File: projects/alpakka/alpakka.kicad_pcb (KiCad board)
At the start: 2 copper layers, 130 x 51 mm, 82 parts, among them P1 Conn_01x20_Pin, P2 Conn_01x20_Pin, P3 Conn_01x04, P4 Blade, P6 Conn_01x02, U1 Alpsalpine_RKJXV, U10 ST_LSM6, U12 ST_LSM6, U2 Alpsalpine_RKJXV, U3 Alpsalpine_EC10E, U6 NXP_PCAL6416A, U8 NXP_PCAL6416A

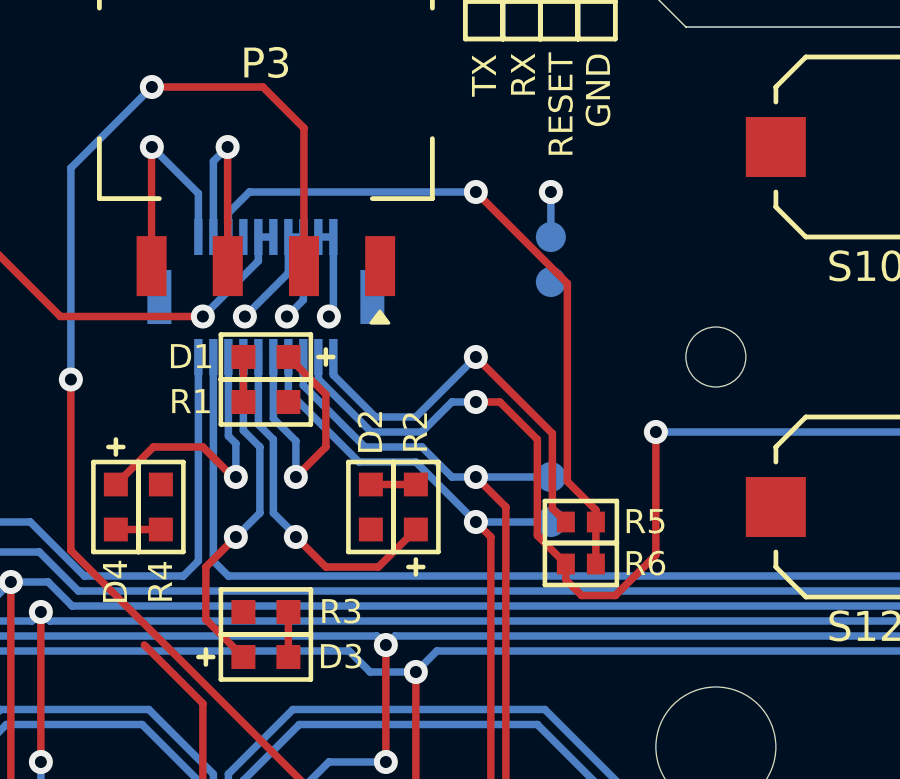
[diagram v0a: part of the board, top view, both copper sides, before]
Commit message: Alpakka revert to single touch path, Shifted GPIOs to match Marmota
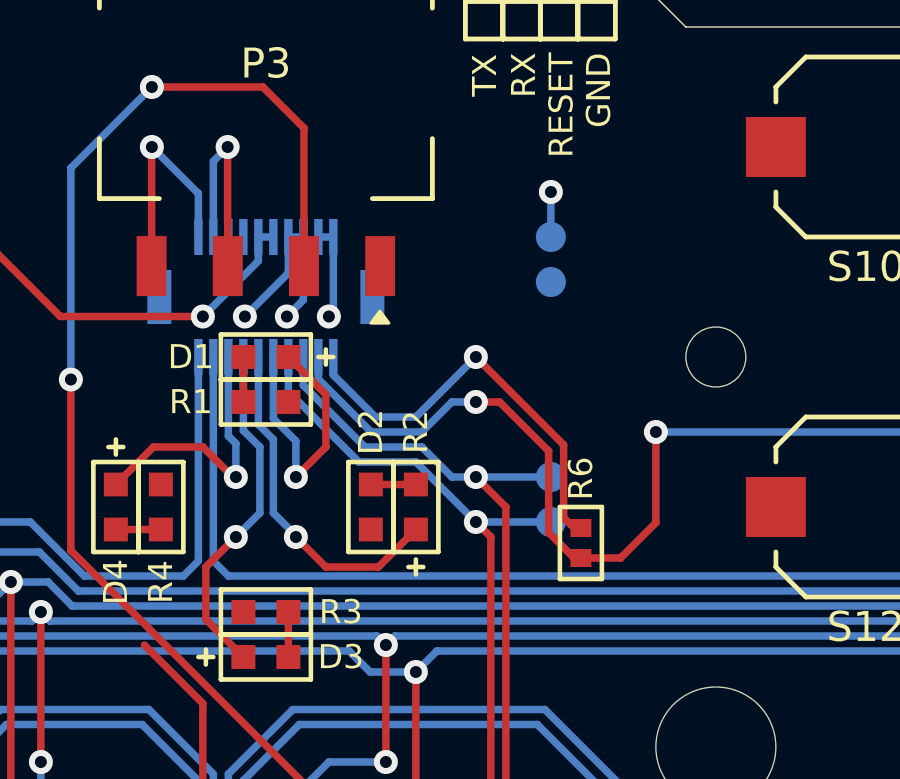
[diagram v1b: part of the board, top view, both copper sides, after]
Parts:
- removed R5: 1 MΩ, ILO_fp:0402
- moved R6 0.70 mm to (110.5, 55.2), turned to 90 degrees
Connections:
- D1 pad 2: /GP10 -> /GP9
- D2 pad 2: /GP9 -> /GP8
- D3 pad 2: /GP8 -> /GP7
- D4 pad 2: /GP7 -> /GP6
- P1 pad 13: /GP7 -> /GP6
- P1 pad 14: /GP8 -> /GP7
- P1 pad 15: /GP9 -> /GP8
- P1 pad 16: /GP10 -> /GP9
- P1 pad 17: /GP11 -> /GP10
- P1 pad 18: /GP12 -> /GP11
- P1 pad 19: /GP13 -> /GP12
- P1 pad 20: /GP14 -> /GP13
- P1 pad 3: /GP4 -> unconnected-(P1-Pin_3-Pad3)
- P4 pad 1: /GP13 -> /GP12
- R6 pad 1: /GP13 -> /GP12
- R6 pad 2: /GP4 -> /GP13
- TPS0 pad 1: /GP11 -> /GP10
- TPS1 pad 1: /GP12 -> /GP11
- U3 pad 1: /GP11 -> /GP10
- U3 pad 2: /GP12 -> /GP11
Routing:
- net /GP13: track 62.7 -> 14.0 mm, vias 3 -> 1
- net /GP10: track 9.24 -> 36.8 mm
- net /GP12: track 35.5 -> 60.5 mm, vias 1 -> 3
- net /GP4: track 23.5 -> 0.00 mm, vias 1 -> 0
- net /GP14: track 13.5 -> 0.00 mm, vias 1 -> 0
- net /GP6: track 0.00 -> 9.04 mm, vias 0 -> 1
- net /GP7: track 9.04 -> 11.5 mm
- net /GP9: track 11.4 -> 9.24 mm
- net /GP11: track 36.8 -> 35.5 mm

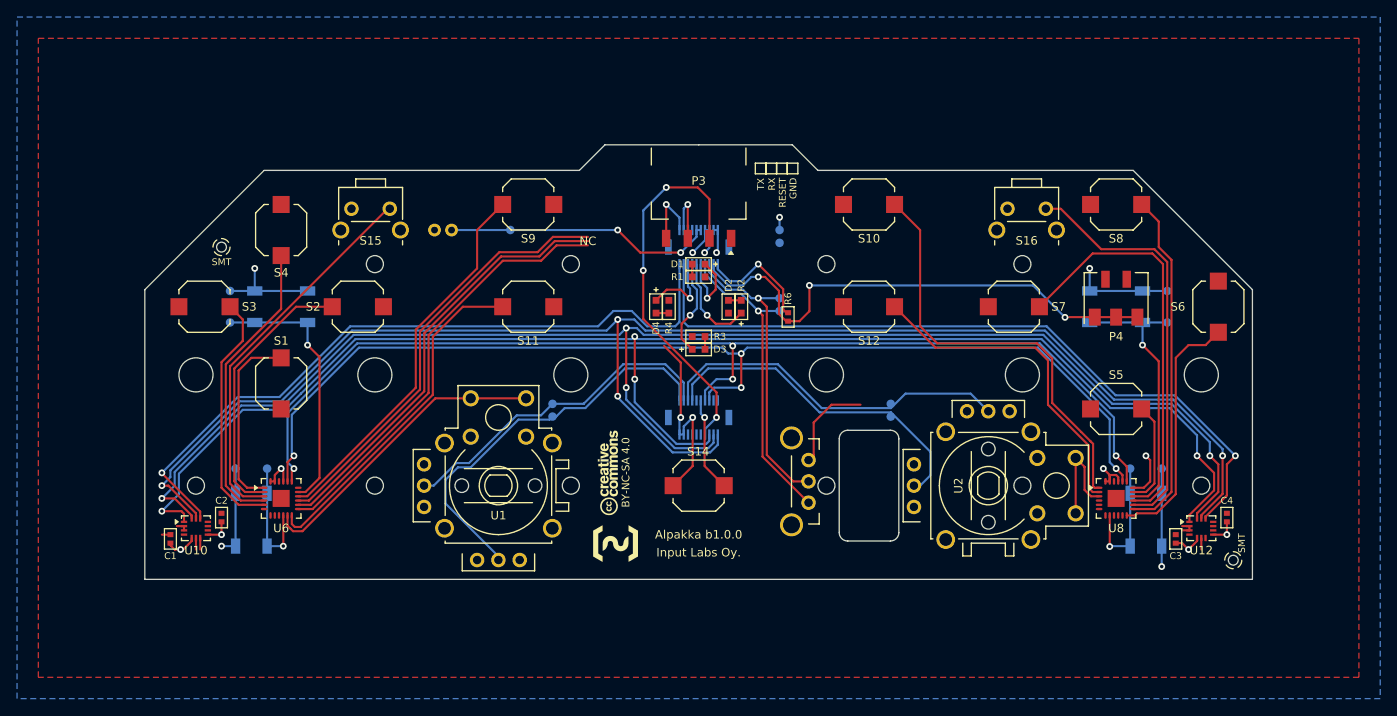
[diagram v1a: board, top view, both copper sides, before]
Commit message: Alpakka edge rails, USB indication silkscreen
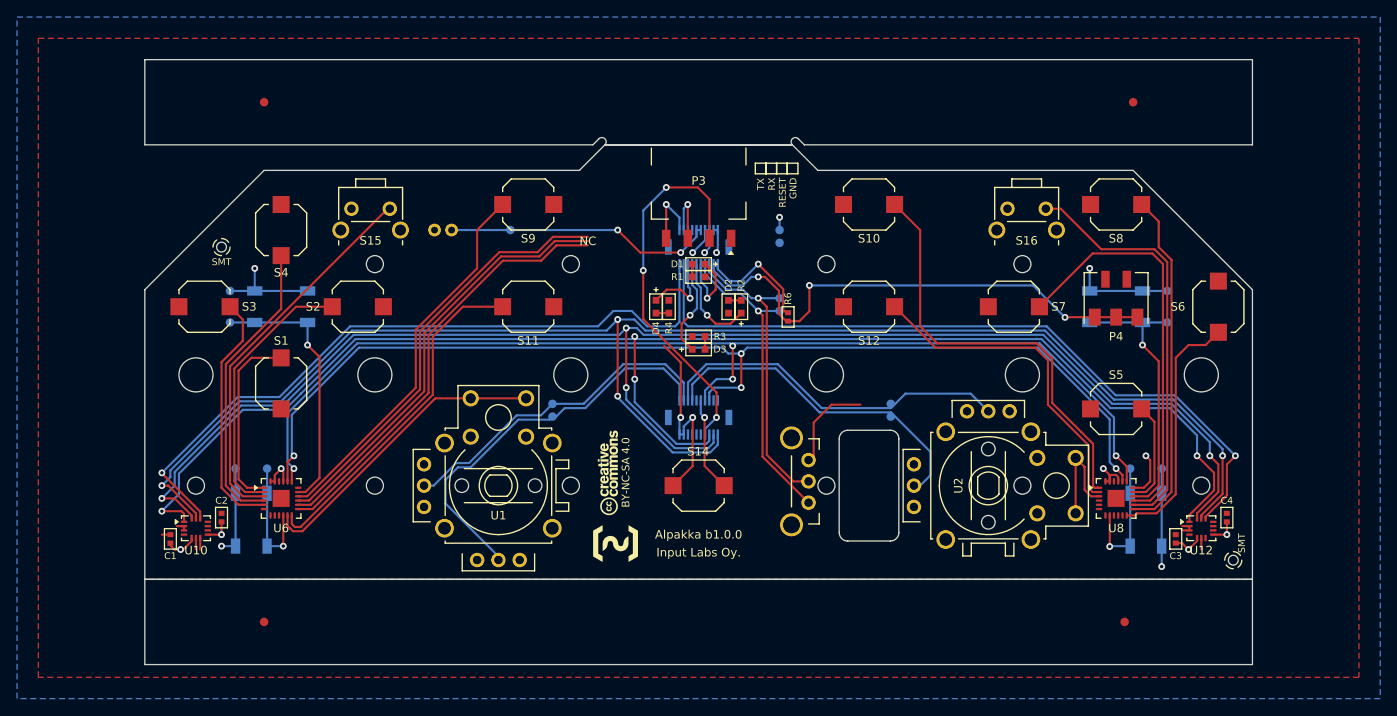
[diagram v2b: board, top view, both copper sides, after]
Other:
- board size 130 x 51 mm -> 130 x 71 mm
- board text added: "--V-CUT"
- board text added: "USB (DNP)"
- board text added: "V-CUT--"

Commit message: Reworked Alpakka w/ interrupt lines, etc
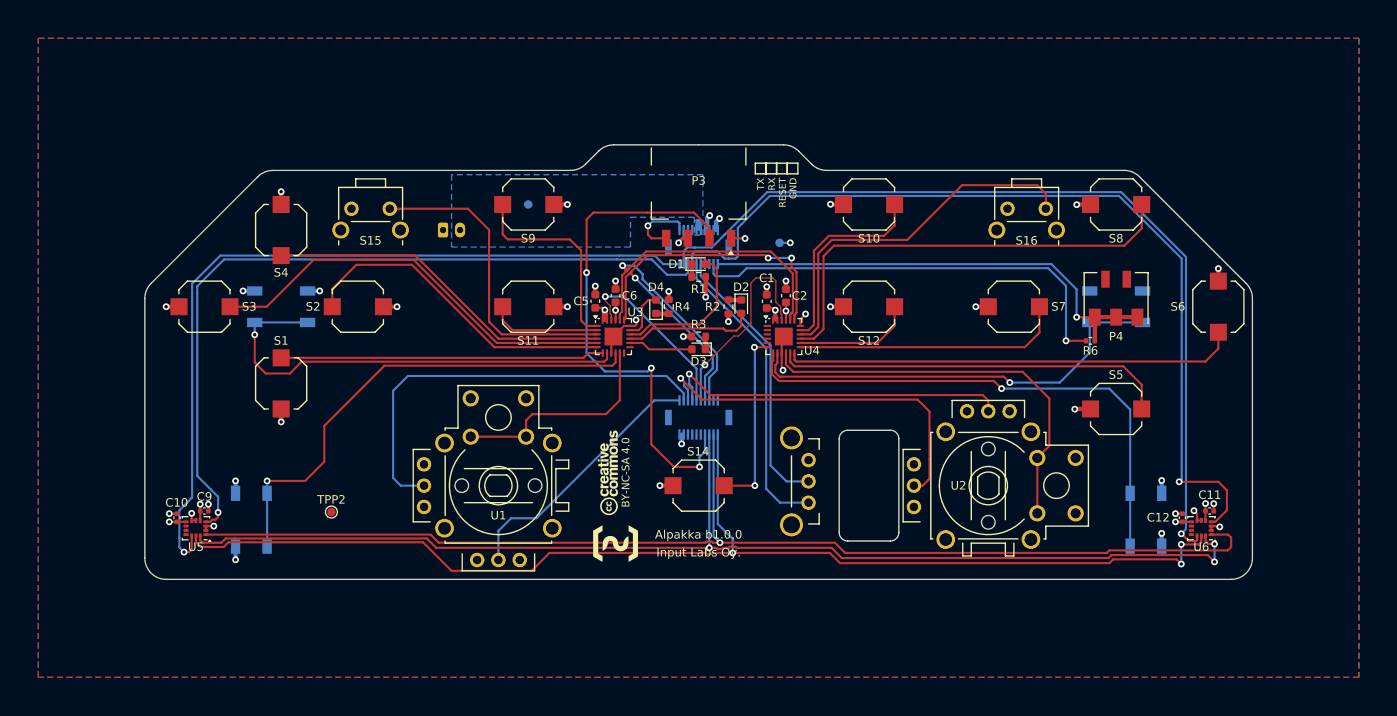
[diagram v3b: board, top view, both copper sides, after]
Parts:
- removed ?: , 
- removed C3, C4: 100nF, ILO_fp:0402
- removed REF** (x6): NPTH_4mm, ILO_fp:NPTH_4mm
- removed REF** (x11): NPTH_2mm, ILO_fp:NPTH_2mm
- removed TP101, TP102, TP103, TP104, TP201, TP202, TP203, TP204, TPA0, TPA1, TPA2, TPA3, TPBAT0, TPP0, TPS0, TPS1: Endpoint, ILO_fp:Pad_1mm
- added C10: 100nF, Capacitor_SMD:C_0402_1005Metric, F.Cu at (38.8, 78.8)
- added C11: 100nF, Capacitor_SMD:C_0402_1005Metric, F.Cu at (160.0, 78.0)
- added C12: 100nF, Capacitor_SMD:C_0402_1005Metric, F.Cu at (156.8, 78.8)
- added C5: 4.7uF, Capacitor_SMD:C_0603_1608Metric, F.Cu at (87.9, 53.4)
- added C6: 4.7uF, Capacitor_SMD:C_0603_1608Metric, F.Cu at (90.2, 52.7)
- added C9: 100nF, Capacitor_SMD:C_0402_1005Metric, F.Cu at (42.0, 78.0)
- added TPP2: Endpoint, TestPoint:TestPoint_Pad_D1.0mm, F.Cu at (56.9, 78.1)
- added TPP3: Endpoint, TestPoint:TestPoint_Pad_D1.0mm, B.Cu at (80.0, 42.0)
- C1, C2: value 100nF -> 4.7uF; footprint ILO_fp:0402 -> Capacitor_SMD:C_0603_1608Metric
- D1, D2, D3, D4: footprint ILO_fp:0603_d -> Diode_SMD:D_0603_1608Metric
- P6: footprint ILO_fp:JST_PH_2_TH -> Connector_JST:JST_PH_S2B-PH-K_1x02_P2.00mm_Horizontal
- R1, R2, R3, R4: footprint ILO_fp:0603 -> Resistor_SMD:R_0603_1608Metric
- R6: footprint ILO_fp:0402 -> Resistor_SMD:R_0402_1005Metric
- SW1: renamed from U3; value Alpsalpine_EC10E -> EC10E
- TPP1: footprint ILO_fp:Pad_1mm -> TestPoint:TestPoint_Pad_D1.0mm
- U3: renamed from U6; value NXP_PCAL6416A -> PCAL6416AHF; footprint ILO_fp:QFN24 -> Package_DFN_QFN:HVQFN-24-1EP_4x4mm_P0.5mm_EP2.1x2.1mm
- U4: renamed from U8; value NXP_PCAL6416A -> PCAL6416AHF; footprint ILO_fp:QFN24 -> Package_DFN_QFN:HVQFN-24-1EP_4x4mm_P0.5mm_EP2.1x2.1mm
- U5: renamed from U10; value ST_LSM6 -> LSM6DSL; footprint ILO_fp:LGA14 -> Package_LGA:LGA-14_3x2.5mm_P0.5mm_LayoutBorder3x4y
- U6: renamed from U12; value ST_LSM6 -> LSM6DSL; footprint ILO_fp:LGA14 -> Package_LGA:LGA-14_3x2.5mm_P0.5mm_LayoutBorder3x4y
- moved C1 75.3 mm to (108.0, 53.4), turned to 90 degrees
- moved C2 71.2 mm to (110.2, 52.7), turned to 90 degrees
- moved U3 43.4 mm to (90.0, 57.5), turned to 0 degrees
- moved U4 43.4 mm to (110.0, 57.5), turned to 0 degrees
- moved R6 35.6 mm to (146.0, 58.0), turned to 180 degrees
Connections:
- net /A2 renamed /B_L1
- net /A3 renamed /B_UP
- net /A4 renamed /B_LEFT
- net /A8 renamed /B_L4
- net /ADC2 renamed /LSTICK_X
- net /ADC3 renamed /LSTICK_Y
- net /B10 renamed /B_B
- net /BAT renamed VBAT
- net /IMU_CS0 renamed /IMU0_~{CS}
- net /IMU_CS1 renamed /IMU1_~{CS}
- net /SPI_CK renamed /SPI_SCK
- C1 pad 1: /GND -> VDD
- C1 pad 2: /VCC -> GND
- C2 pad 1: /GND -> VDD
- C2 pad 2: /VCC -> GND
- D1 pad 2: /GP9 -> /LED1
- D2 pad 2: /GP8 -> /LED2
- D3 pad 2: /GP7 -> /LED3
- D4 pad 2: /GP6 -> /LED4
- P1 pad 10: /VCC -> VDD
- P1 pad 13: /GP6 -> /IMU0_~{INT}
- P1 pad 14: /GP7 -> /IMU1_~{INT}
- P1 pad 15: /GP8 -> /SCROLL_A
- P1 pad 16: /GP9 -> /SCROLL_B
- P1 pad 19: /GP12 -> /TOUCH_STIM
- P1 pad 20: /GP13 -> /TOUCH_MEAS
- P1 pad 7: /GND -> GND
- P1 pad 8: /GND -> GND
- P1 pad 9: /VCC -> VDD
- P2 pad 11: /GND -> GND
- P2 pad 12: /GND -> GND
- P2 pad 18: /SPI_RX -> /SPI_SDO
- P2 pad 19: /SPI_TX -> /SPI_SDI
- P2 pad 3: /ADC1 -> /RSTICK_Y
- P2 pad 4: /ADC0 -> /RSTICK_X
- P2 pad 5: /GP25 -> /EXP0_~{INT}
- P2 pad 6: /GP24 -> /EXP1_~{INT}
- P3 pad 1: /GND -> GND
- P4 pad 1: /GP12 -> /TOUCH_MEAS
- P6 pad 1: /GND -> GND
- R1 pad 1: /GND -> GND
- R2 pad 1: /GND -> GND
- R3 pad 1: /GND -> GND
- R4 pad 1: /GND -> GND
- R6 pad 1: /GP12 -> /TOUCH_MEAS
- R6 pad 2: /GP13 -> /TOUCH_STIM
- S1 pad 1: /GND -> GND
- S1 pad 2: /A0 -> /B_DOWN
- S10 pad 1: /GND -> GND
- S10 pad 2: /B0 -> /B_START1
- S11 pad 1: /GND -> GND
- S11 pad 2: /A10 -> /B_SEL2
- S12 pad 1: /GND -> GND
- S12 pad 2: /B1 -> /B_START2
- S14 pad 1: /GND -> GND
- S14 pad 2: /GP24 -> /B_HOME
- S15 pad 1: /GND -> GND
- S16 pad 1: /GND -> GND
- S16 pad 2: /B12 -> /B_R1
- S17 pad 1: /GND -> GND
- S17 pad 2: /A15 -> /B_L2
- S18 pad 1: /GND -> GND
- S18 pad 2: /B14 -> /B_R2
- S19 pad 1: /GND -> GND
- S2 pad 1: /GND -> GND
- S2 pad 2: /A1 -> /B_RIGHT
- S20 pad 1: /GND -> GND
- S20 pad 2: /B7 -> /B_R4
- S3 pad 1: /GND -> GND
- S4 pad 1: /GND -> GND
- S5 pad 1: /GND -> GND
- S5 pad 2: /B15 -> /B_A
- S6 pad 1: /GND -> GND
- S7 pad 1: /GND -> GND
- S7 pad 2: /B13 -> /B_X
- S8 pad 1: /GND -> GND
- S8 pad 2: /B11 -> /B_Y
- S9 pad 1: /GND -> GND
- S9 pad 2: /A14 -> /B_SEL1
- TPP1 pad 1: /VCC -> VDD
- U1 pad 1: /GND -> GND
- U1 pad 10: /A9 -> GND
- U1 pad 3: /VCC -> VDD
- U1 pad 4: /GND -> GND
- U1 pad 6: /VCC -> VDD
- U1 pad 7: /GND -> /LSTICK_PUSH
- U1 pad 8: /A9 -> GND
- U1 pad 9: /GND -> /LSTICK_PUSH
- U2 pad 1: /GND -> GND
- U2 pad 10: /B2 -> GND
- U2 pad 2: /ADC1 -> /RSTICK_X
- U2 pad 3: /VCC -> VDD
- U2 pad 4: /GND -> GND
- U2 pad 5: /ADC0 -> /RSTICK_Y
- U2 pad 6: /VCC -> VDD
- U2 pad 7: /GND -> /RSTICK_PUSH
- U2 pad 8: /B2 -> GND
- U2 pad 9: /GND -> /RSTICK_PUSH
- U3 pad 1: /A0 -> /B_SEL1
- U3 pad 11: /A9 -> /LSTICK_PUSH
- U3 pad 12: /A10 -> unconnected-(U3-P1_2-Pad12)
- U3 pad 13: /A11 -> unconnected-(U3-P1_3-Pad13)
- U3 pad 14: /A12 -> /LED3
- U3 pad 15: /A13 -> /LED2
- U3 pad 16: /A14 -> /LED1
- U3 pad 17: /A15 -> /LED4
- U3 pad 18: /GND -> GND
- U3 pad 2: /A1 -> /B_SEL2
- U3 pad 21: /VCC -> VDD
- U3 pad 22: unconnected-(U6-INT-Pad22) -> /EXP0_~{INT}
- U3 pad 23: /VCC -> VDD
- U3 pad 24: /VCC -> VDD
- U3 pad 6: unconnected-(U6-P5-Pad6) -> /B_RIGHT
- U3 pad 7: /A6 -> /B_DOWN
- U3 pad 8: /A7 -> /B_L2
- U3 pad 9: /GND -> GND
- U4 pad 1: /B0 -> unconnected-(U4-P0_0-Pad1)
- U4 pad 10: unconnected-(U8-P8-Pad10) -> /RSTICK_PUSH
- U4 pad 11: unconnected-(U8-P9-Pad11) -> /B_A
- U4 pad 13: /B11 -> /B_X
- U4 pad 14: /B12 -> /B_START2
- U4 pad 15: /B13 -> /B_Y
- U4 pad 16: /B14 -> /B_R1
- U4 pad 17: /B15 -> /B_START1
- U4 pad 18: /VCC -> VDD
- U4 pad 2: /B1 -> unconnected-(U4-P0_1-Pad2)
- U4 pad 21: /VCC -> VDD
- U4 pad 22: unconnected-(U8-INT-Pad22) -> /EXP1_~{INT}
- U4 pad 23: /VCC -> VDD
- U4 pad 24: /VCC -> VDD
- U4 pad 3: /B2 -> unconnected-(U4-P0_2-Pad3)
- U4 pad 4: /B3 -> unconnected-(U4-P0_3-Pad4)
- U4 pad 5: /B4 -> unconnected-(U4-P0_4-Pad5)
- U4 pad 6: /B5 -> /B_HOME
- U4 pad 7: /B6 -> /B_R4
- U4 pad 8: /B7 -> /B_R2
- U4 pad 9: /GND -> GND
- U5 pad 1: /SPI_RX -> /SPI_SDI
- U5 pad 14: /SPI_TX -> /SPI_SDO
- U5 pad 2: /GND -> GND
- U5 pad 3: /GND -> GND
- U5 pad 4: unconnected-(U10-INT1-Pad4) -> /IMU0_~{INT}
- U5 pad 5: /VCC -> VDD
- U5 pad 6: /GND -> GND
- U5 pad 7: /GND -> GND
- U5 pad 8: /VCC -> VDD
- U6 pad 1: /SPI_RX -> /SPI_SDI
- U6 pad 14: /SPI_TX -> /SPI_SDO
- U6 pad 2: /GND -> GND
- U6 pad 3: /GND -> GND
- U6 pad 4: unconnected-(U12-INT1-Pad4) -> /IMU1_~{INT}
- U6 pad 5: /VCC -> VDD
- U6 pad 6: /GND -> GND
- U6 pad 7: /GND -> GND
- U6 pad 8: /VCC -> VDD
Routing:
- net /SPI_TX: track 175.1 -> 0.00 mm, vias 4 -> 0
- net /SPI_RX: track 171.4 -> 0.00 mm, vias 4 -> 0
- net /SPI_SDO: track 0.00 -> 138.7 mm, vias 0 -> 3
- net /SPI_SDI: track 0.00 -> 138.2 mm, vias 0 -> 1
- net /IMU1_~{INT}: track 0.00 -> 104.2 mm, vias 0 -> 1
- net /GND: track 96.5 -> 0.00 mm, vias 9 -> 0
- net /IMU0_~{INT}: track 0.00 -> 90.5 mm, vias 0 -> 1
- net /I2C_SCL: track 129.6 -> 53.4 mm, vias 4 -> 3
- net /I2C_SDA: track 128.4 -> 56.4 mm, vias 4 -> 1
- net GND: track 0.00 -> 62.9 mm, vias 0 -> 40
- net /B_R4: track 0.00 -> 62.3 mm, vias 0 -> 1
- net /GP12: track 60.5 -> 0.00 mm, vias 3 -> 0
- net /TOUCH_MEAS: track 0.00 -> 56.5 mm, vias 0 -> 1
- net /B_L2: track 0.00 -> 54.2 mm, vias 0 -> 1
- net /B_Y: track 0.00 -> 53.2 mm
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- added copper zone on B.Cu, net GND
- added copper zone on F.Cu, net GND
- added copper zone on In1.Cu, net GND
- added copper zone on B.Cu, net VBAT
- added copper zone on In2.Cu, net VDD
- removed copper zone on F.Cu, net /GND
- removed copper zone on B.Cu, net /VCC
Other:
- board size 130 x 71 mm -> 130 x 51 mm
- copper layers 2 -> 4
- board text removed: "--V-CUT"
- board text removed: "BAT"
- board text removed: "NC"
- board text removed: "SMT"
- board text removed: "TP"
- board text removed: "USB (DNP)"
- board text removed: "V-CUT--"

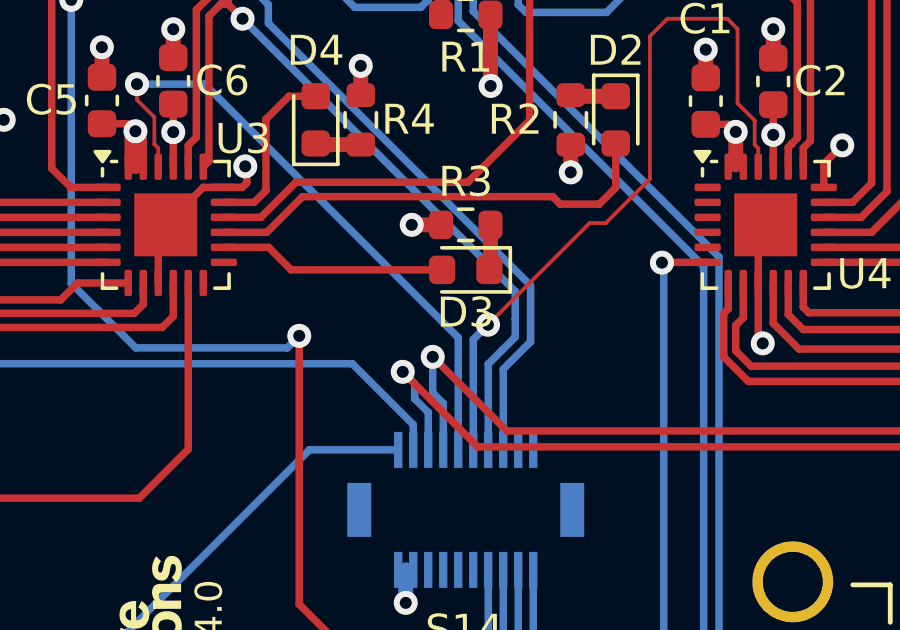
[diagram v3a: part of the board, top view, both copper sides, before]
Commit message: Updated for nRF52840
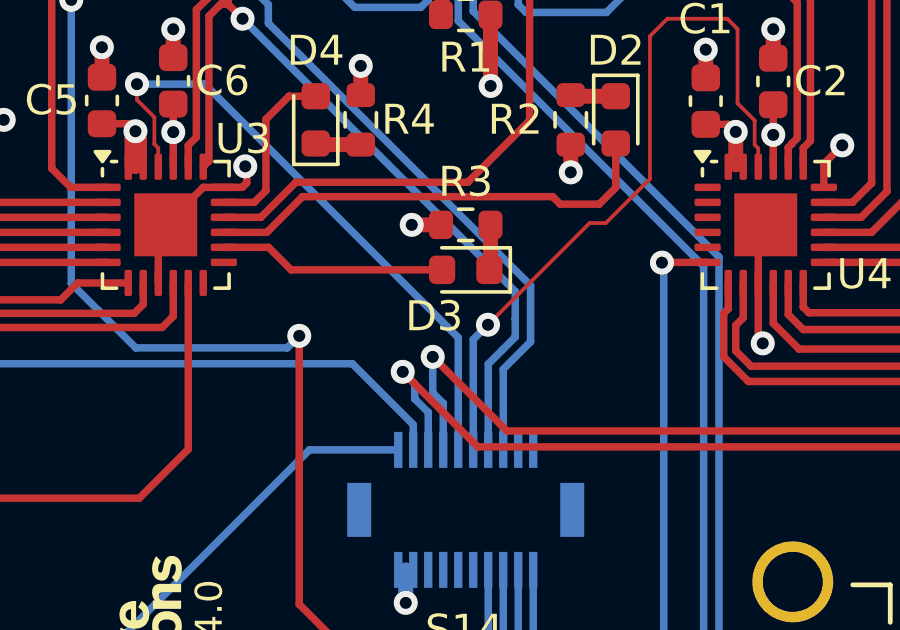
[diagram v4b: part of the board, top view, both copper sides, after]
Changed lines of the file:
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@@
 		(tags "diode")
 		(property "Reference" "D3"
-			(at 0 -1.43 180)
+			(at 1.05 -1.55 180)
 			(layer "F.SilkS")
 			(effects
